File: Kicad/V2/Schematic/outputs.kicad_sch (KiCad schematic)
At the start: 20 parts, among them U4 TUSB321

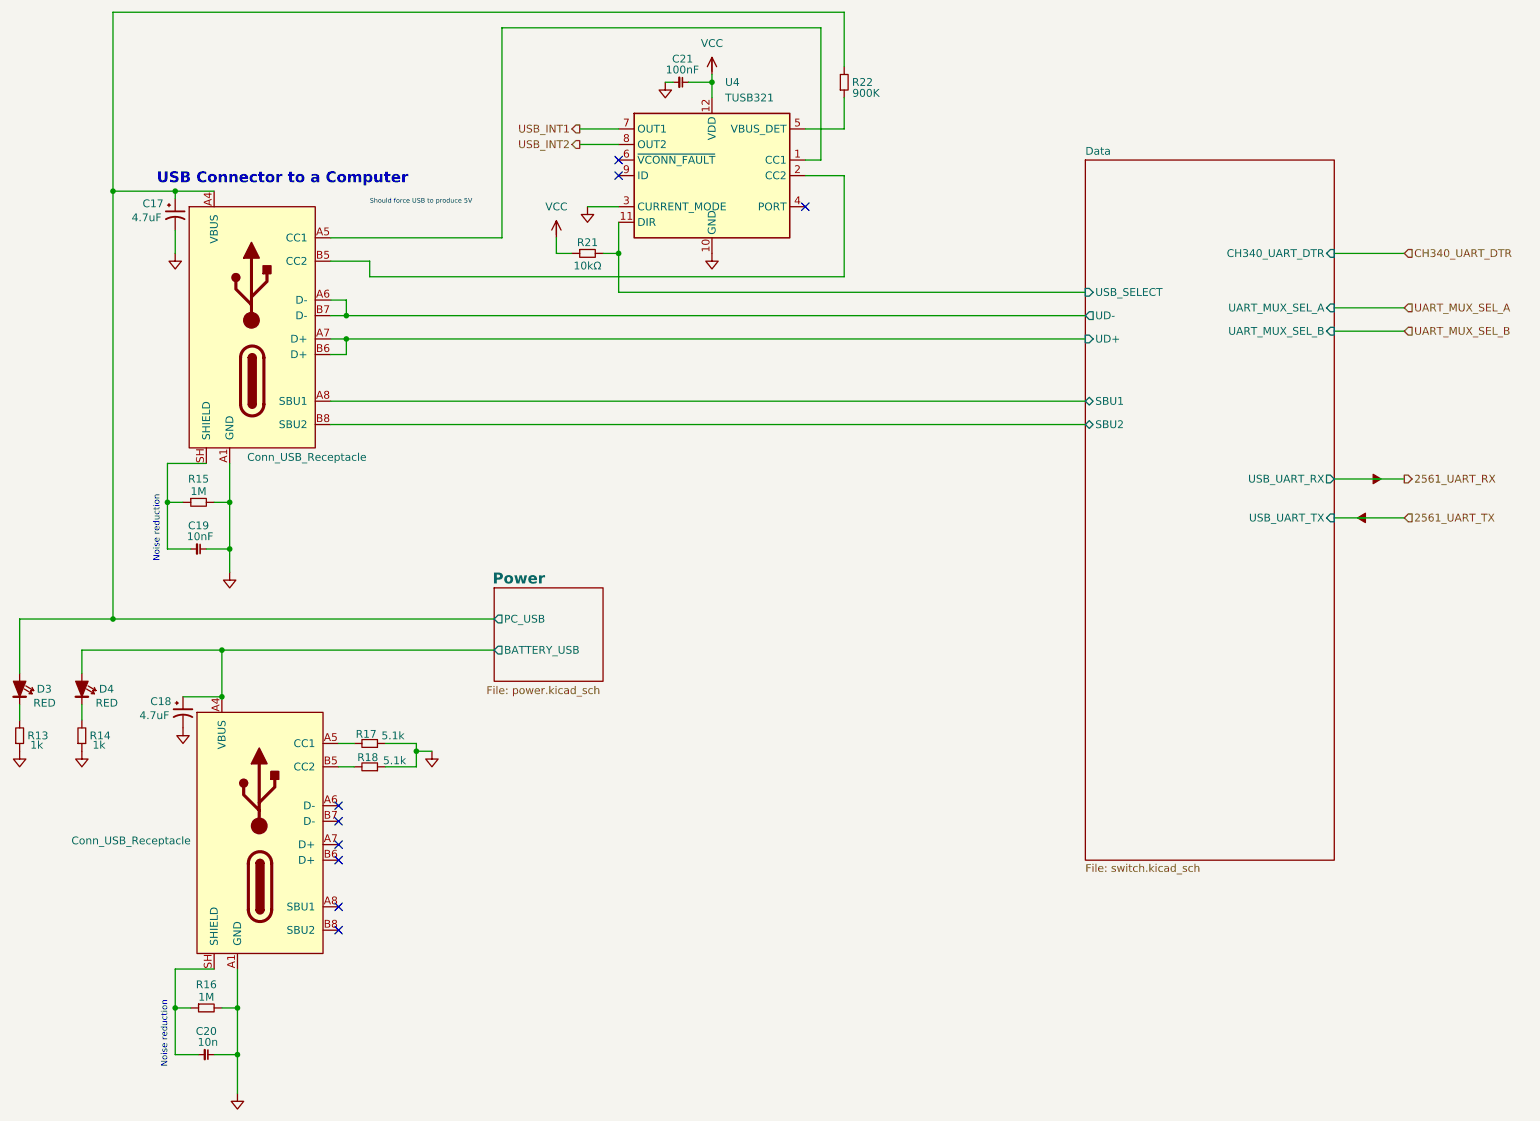
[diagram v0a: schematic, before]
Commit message: Split power and data
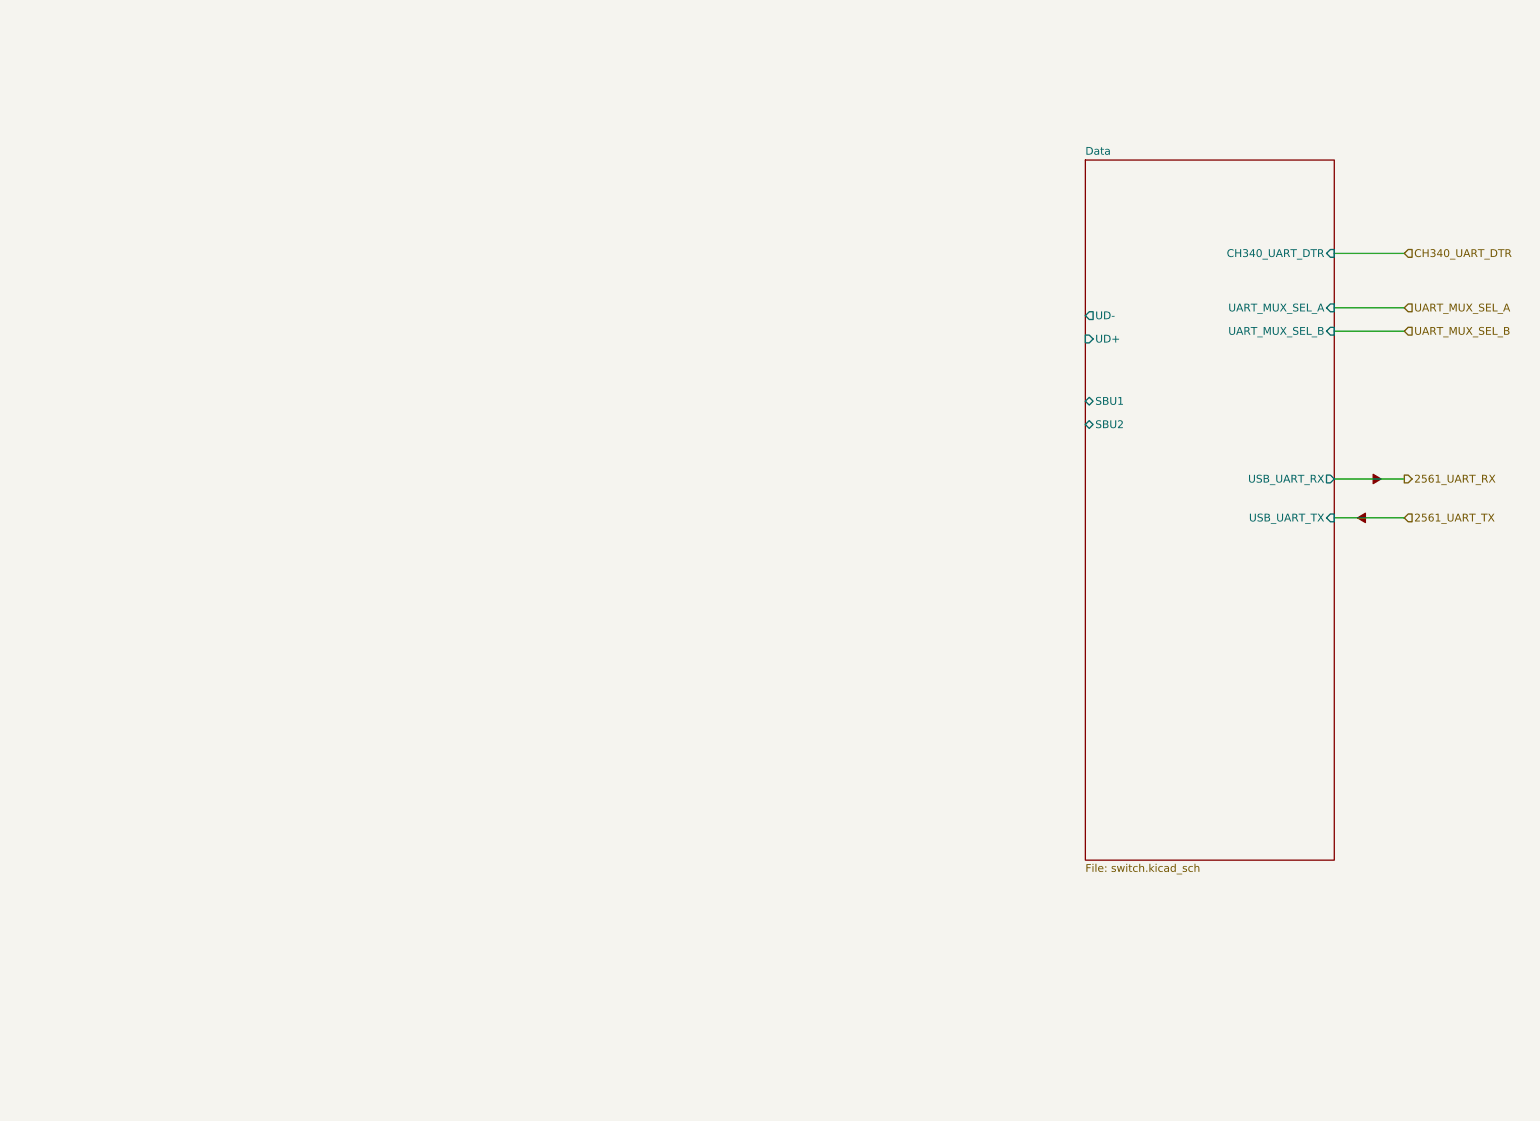
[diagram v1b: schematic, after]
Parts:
- removed C17, C18: 4.7uF, MyGlove:Capacitor_Electrolytic, symbol Device:C_Polarized_Small_US
- removed C19: 10nF, MyGlove:Capacitor_0603, symbol G-Love:C
- removed C20: 10n, MyGlove:Capacitor_0603, symbol G-Love:C
- removed C21: 100nF, MyGlove:Capacitor_0603, symbol G-Love:C
- removed D3, D4: RED, MyGlove:LED, symbol G-Love:LED_Indicator
- removed J_1: Conn_USB_Receptacle, MyGlove:USB_C_Receptacle_GCT_USB4105-xx-A_16P_TopMnt_Horizontal, symbol G-Love:J_USB_RECEPTACLE
- removed J_2: Conn_USB_Receptacle, MyGlove:USB_C_Receptacle_GCT_USB4105-xx-A_16P_TopMnt_Horizontal, symbol G-Love:J_USB_RECEPTACLE_PASSIVE
- removed R13, R14: 1k, MyGlove:Resistor_0603, symbol G-Love:R
- removed R15, R16: 1M, MyGlove:Resistor_0603, symbol G-Love:R
- removed R17, R18: 5.1k, MyGlove:Resistor_0603, symbol G-Love:R
- removed R21: 10kΩ, MyGlove:Resistor_0603, symbol G-Love:R
- removed R22: 900K, MyGlove:Resistor_0805, symbol G-Love:R
- removed U4: TUSB321, Package_DFN_QFN:Texas_X2QFN-12_1.6x1.6mm_P0.4mm, symbol Interface_USB:TUSB321
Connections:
- no-connect marks 9 -> 0
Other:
- removed sheet Power
- sheet Data ports: added none; removed USB_SELECT
- note removed: "Noise reduction"
- note removed: "Should force USB to produce 5V"
- note removed: "USB Connector to a Computer"
